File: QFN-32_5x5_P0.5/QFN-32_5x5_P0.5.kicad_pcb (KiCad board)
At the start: 2 copper layers, 25.4 x 45.7 mm, 6 parts, among them J101 Conn_01x26, J102 Conn_01x26, J103 Conn_01x26, J104 Conn_01x26, U101 QFN-48

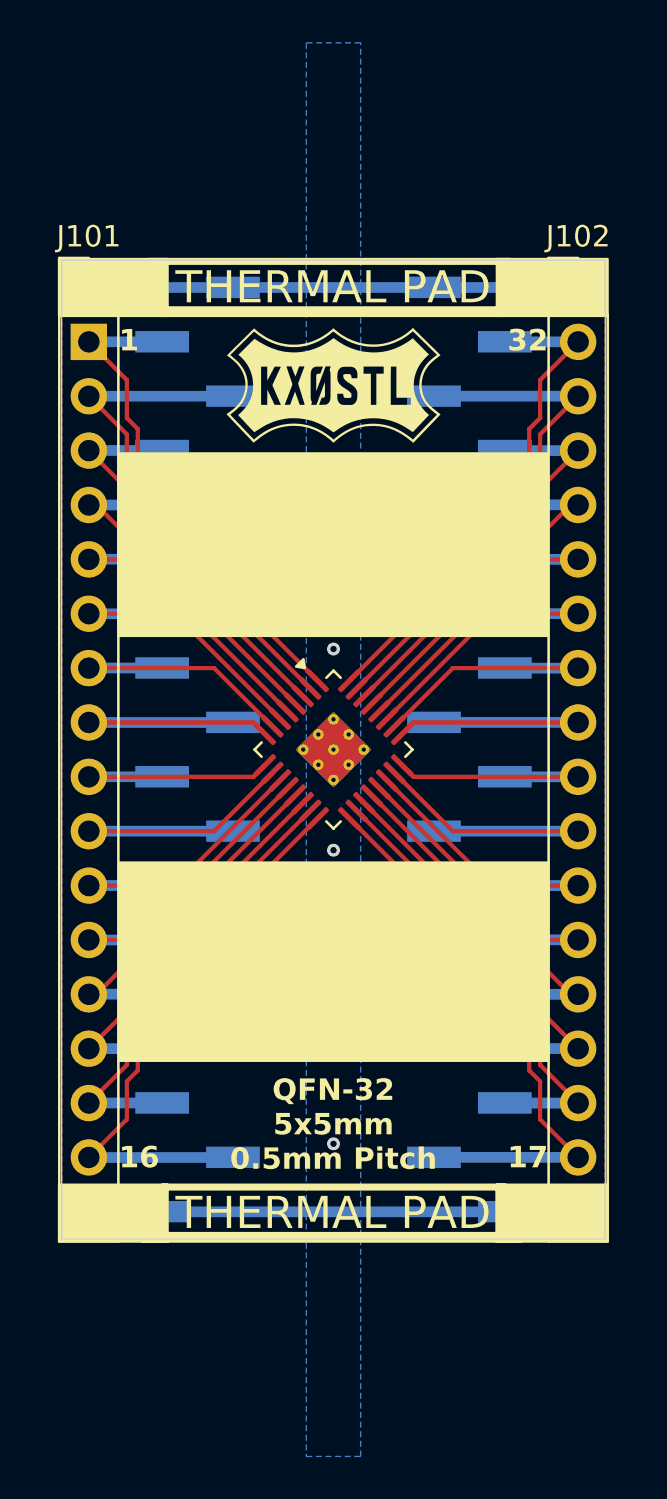
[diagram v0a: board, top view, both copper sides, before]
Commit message: Created SMDIP-16, QFP-48, QFP-32, QFN-80, QFN-68, QFN-64, QFN-60, QFN-56, QFN-48, QFN-36, QFN-28, QFN-20, QFP-32, QFP-48
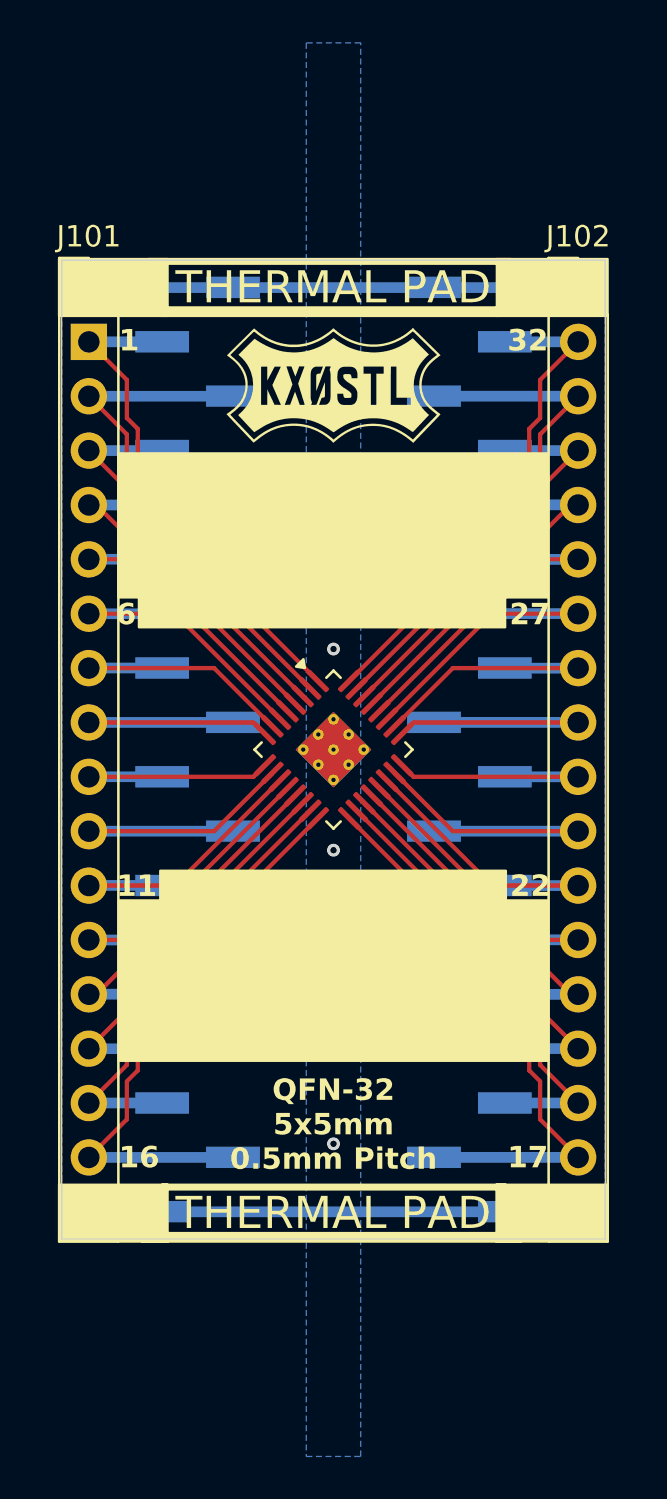
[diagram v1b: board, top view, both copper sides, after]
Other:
- board text added: "11"
- board text added: "22"
- board text added: "27"
- board text added: "6"
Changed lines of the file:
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@@
+	)
+	(gr_rect
+		(start 130.332 126.3056)
+		(end 146.488 128.91)
+		(stroke
+			(width 0.1)
+			(type solid)
+		)
+		(fill yes)
+		(layer "F.SilkS")
 	)
 	(gr_rect
@@
 	(gr_rect
 		(start 128.36935 106.807)
-		(end 148.43535 115.3414)
+		(end 148.43535 113.5414)
 		(stroke
 			(width 0.1)
@@
 	)
 	(gr_rect
-		(start 128.397 125.9205)
+		(start 128.397 127.6905)
 		(end 148.463 135.1915)
 		(stroke
@@
 	)
 	(gr_rect
+		(start 129.337 108.1856)
+		(end 146.453 114.94)
+		(stroke
+			(width 0.1)
+			(type solid)
+		)
+		(fill yes)
+		(layer "F.SilkS")
+	)
+	(gr_rect
 		(start 146.05425 97.726375)
 		(end 151.24 100.393625)
@@
 		)
 	)
+	(gr_text "6"
+		(at 128.26 114.33 0)
+		(layer "F.SilkS" knockout)
+		(effects
+			(font
+				(size 1 1)
+				(thickness 0.2)
+				(bold yes)
+			)
+			(justify left)
+		)
+	)
 	(gr_text "17"
 		(at 148.463 139.7 0)
@@
 		)
 	)
+	(gr_text "11"
+		(at 128.28 127.02 0)
+		(layer "F.SilkS" knockout)
+		(effects
+			(font
+				(size 1 1)
+				(thickness 0.2)
+				(bold yes)
+			)
+			(justify left)
+		)
+	)
 	(gr_text "THERMAL PAD"
 		(at 138.4215 142.303375 0)
@@
 		)
 	)
+	(gr_text "27"
+		(at 148.56 114.33 0)
+		(layer "F.SilkS" knockout)
+		(effects
+			(font
+				(size 1 1)
+				(thickness 0.2)
+				(bold yes)
+			)
+			(justify right)
+		)
+	)
 	(gr_text "THERMAL PAD"
 		(at 138.4215 99.06 0)
@@
 		)
 	)
+	(gr_text "22"
+		(at 148.58 127.02 0)
+		(layer "F.SilkS" knockout)
+		(effects
+			(font
+				(size 1 1)
+				(thickness 0.2)
+				(bold yes)
+			)
+			(justify right)
+		)
+	)
